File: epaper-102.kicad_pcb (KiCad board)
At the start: 2 copper layers, 19.6 x 38.6 mm, 20 parts, among them J1 Conn_01x30_Female, J2 Conn_01x08_Female

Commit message: backup
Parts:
- C1, C10, C11, C13, C15, C16, C17, C2, C3, C4, C5, C6, C7, C8, C9: footprint Capacitor_SMD:C_0402_1005Metric -> Capacitor_SMD:C_0603_1608Metric
- moved C14 2.66 mm to (41.3, 78.1)
- moved C5 2.62 mm to (28.6, 78.0)
- moved C11 2.62 mm to (36.4, 78.0)
- moved C12 2.61 mm to (39.5, 78.1)
- moved C4 2.55 mm to (26.4, 78.1)
- moved C6 2.52 mm to (31.2, 78.2)
- moved C9 2.44 mm to (33.8, 78.2)
- moved C8 2.37 mm to (33.4, 83.2)
- moved C1 2.32 mm to (26.7, 81.7)
- moved C10 2.24 mm to (36.2, 83.3)
- moved C16 2.08 mm to (25.1, 81.6)
- moved C7 1.40 mm to (30.6, 84.3)
- moved C2 0.90 mm to (25.3, 85.8)
- moved C17 0.61 mm to (26.8, 85.8)
- moved C3 0.38 mm to (28.4, 85.8)
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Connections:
- J1 pad 30: Net-(J1-Pad30) -> unconnected-(J1-Pad30)
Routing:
- net GND: track 9.61 -> 18.0 mm, vias 21 -> 13
- net Net-(C11-Pad1): track 11.2 -> 13.9 mm
- net Net-(C6-Pad1): track 11.6 -> 14.3 mm
- net Net-(C8-Pad1): track 6.10 -> 8.71 mm
- net Net-(C9-Pad1): track 11.4 -> 14.0 mm
- net Net-(C12-Pad1): track 9.12 -> 11.7 mm
- net Net-(C12-Pad2): track 10.9 -> 13.5 mm
- net Net-(C14-Pad2): track 9.57 -> 12.1 mm
- net Net-(C5-Pad2): track 10.9 -> 13.3 mm
- net Net-(C10-Pad1): track 5.88 -> 8.27 mm
- net Net-(C11-Pad2): track 9.79 -> 12.1 mm
- net Net-(C6-Pad2): track 10.2 -> 12.5 mm
- net Net-(C8-Pad2): track 4.74 -> 6.96 mm
- net Net-(C9-Pad2): track 10.0 -> 12.2 mm
- net Net-(C4-Pad2): track 11.8 -> 14.0 mm
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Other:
- net class Default removed

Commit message: delete the reset pin
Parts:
- J2: value Conn_01x08_Female -> connector; footprint Connector_PinHeader_2.54mm:PinHeader_1x08_P2.54mm_Vertical -> Connector_PinHeader_2.54mm:PinHeader_1x07_P2.54mm_Vertical; moved to F.Cu
- moved J2 1.27 mm to (25.7, 65.5), turned to 90 degrees
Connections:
- J1 pad 23: RST -> unconnected-(J1-Pad23)
- J2 pad 1: CS -> DC
- J2 pad 2: DC -> GND
- J2 pad 3: GND -> 3V3
- J2 pad 4: 3V3 -> CS
- J2 pad 5: CLK -> DIN
- J2 pad 6: DIN -> CLK
- J2 pad 7: RST -> BUSY
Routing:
- net RST: track 37.1 -> 0.00 mm, vias 1 -> 0
- net CS: track 35.4 -> 37.0 mm
- net CLK: track 35.7 -> 37.2 mm
- net BUSY: track 37.9 -> 37.4 mm
- net 3V3: track 32.0 -> 31.5 mm
- net DC: track 35.0 -> 35.5 mm
- net DIN: track 36.9 -> 36.3 mm
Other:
- board text removed: "RST"

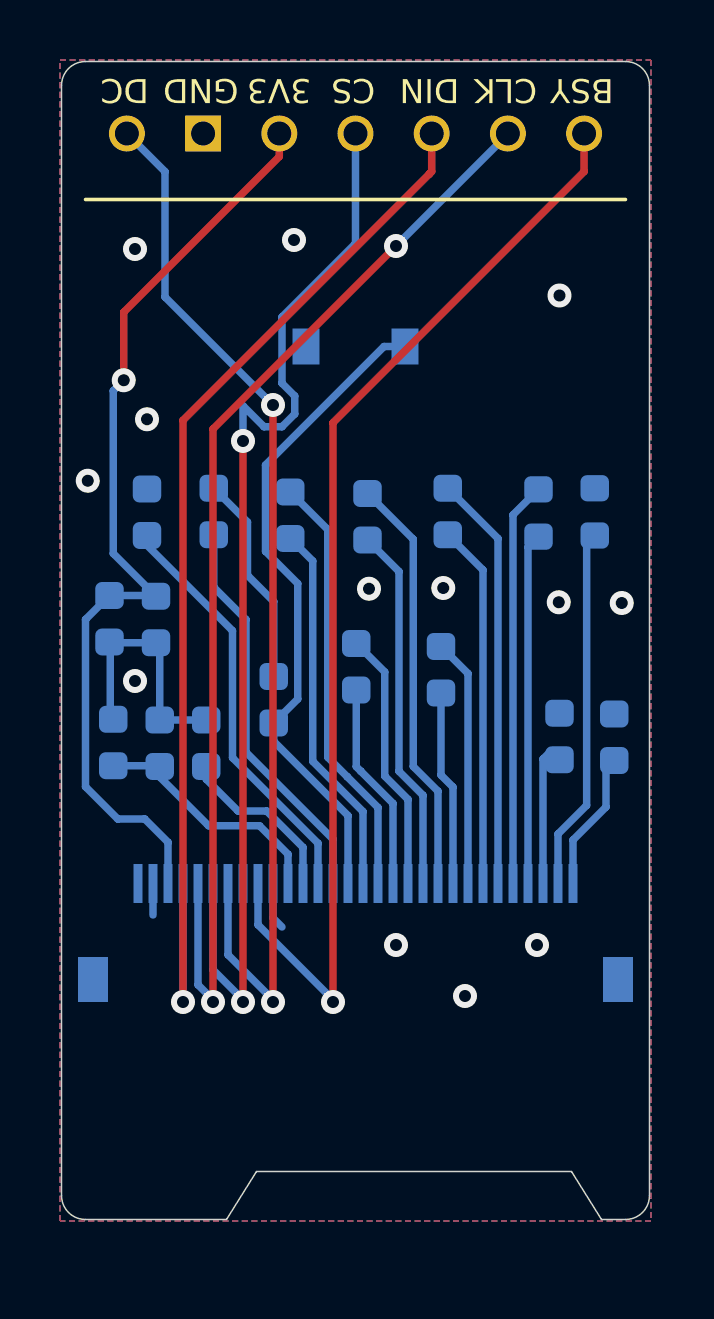
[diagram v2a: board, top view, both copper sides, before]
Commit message: add two mounting socket and optimize the the dimensions
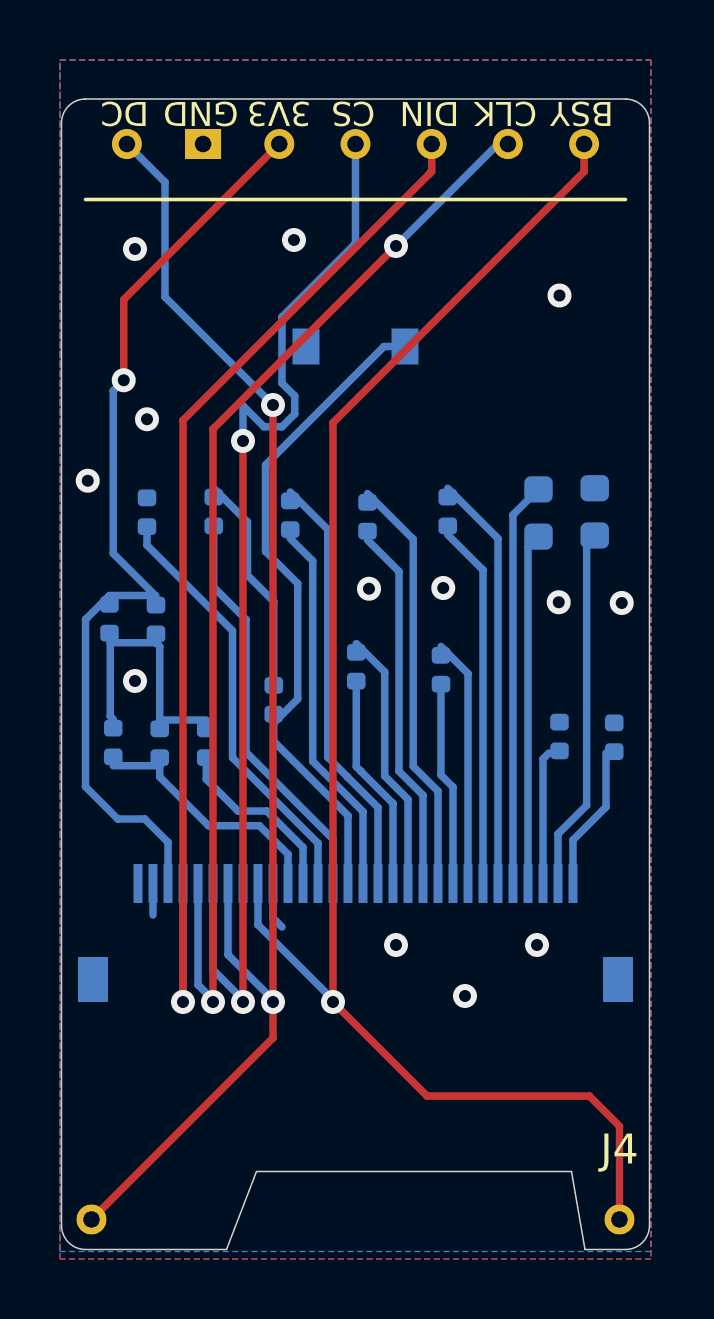
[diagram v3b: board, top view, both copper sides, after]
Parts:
- added J3: Conn_01x01_Female, Connector_PinHeader_2.54mm:PinHeader_1x01_P2.54mm_Vertical, F.Cu at (24.6, 101.7)
- added J4: Conn_01x01_Female, Connector_PinHeader_2.54mm:PinHeader_1x01_P2.54mm_Vertical, F.Cu at (42.1, 101.7)
- C1, C10, C11, C13, C15, C16, C17, C2, C3, C4, C5, C6, C7, C8, C9: footprint Capacitor_SMD:C_0603_1608Metric -> Capacitor_SMD:C_0402_1005Metric
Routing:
- net BUSY: track 37.4 -> 51.8 mm
- net DC: track 35.5 -> 44.9 mm
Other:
- board size 19.6 x 38.6 mm -> 19.6 x 38.4 mm
